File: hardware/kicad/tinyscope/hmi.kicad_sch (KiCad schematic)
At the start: 1 part, among them U10 CR2013-MI2120

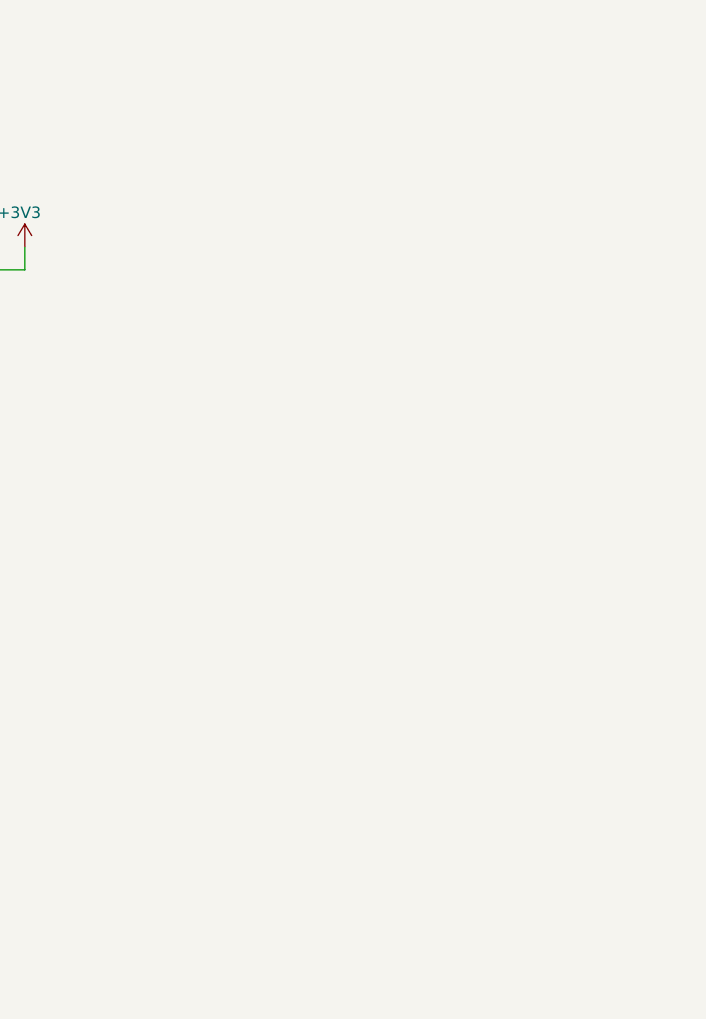
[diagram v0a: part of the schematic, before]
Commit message: feat: hardware: Adds five encoders in HMI schematic #1
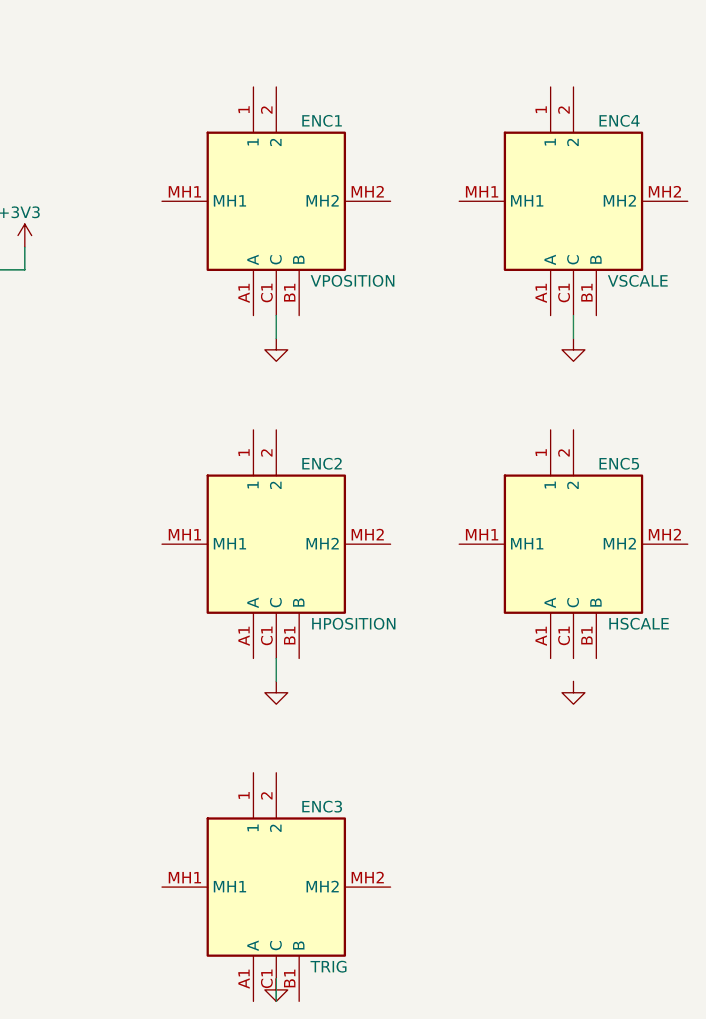
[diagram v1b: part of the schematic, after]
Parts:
- added ENC1: VPOSITION, PEC11R4220FS0024, symbol PEC11R-4220F-S0024:PEC11R-4220F-S0024
- added ENC2: HPOSITION, PEC11R4220FS0024, symbol PEC11R-4220F-S0024:PEC11R-4220F-S0024
- added ENC3: TRIG, PEC11R4220FS0024, symbol PEC11R-4220F-S0024:PEC11R-4220F-S0024
- added ENC4: VSCALE, PEC11R4220FS0024, symbol PEC11R-4220F-S0024:PEC11R-4220F-S0024
- added ENC5: HSCALE, PEC11R4220FS0024, symbol PEC11R-4220F-S0024:PEC11R-4220F-S0024
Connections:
- net GND: now also ENC1.C1 (C), ENC2.C1 (C), ENC3.C1 (C), ENC4.C1 (C)

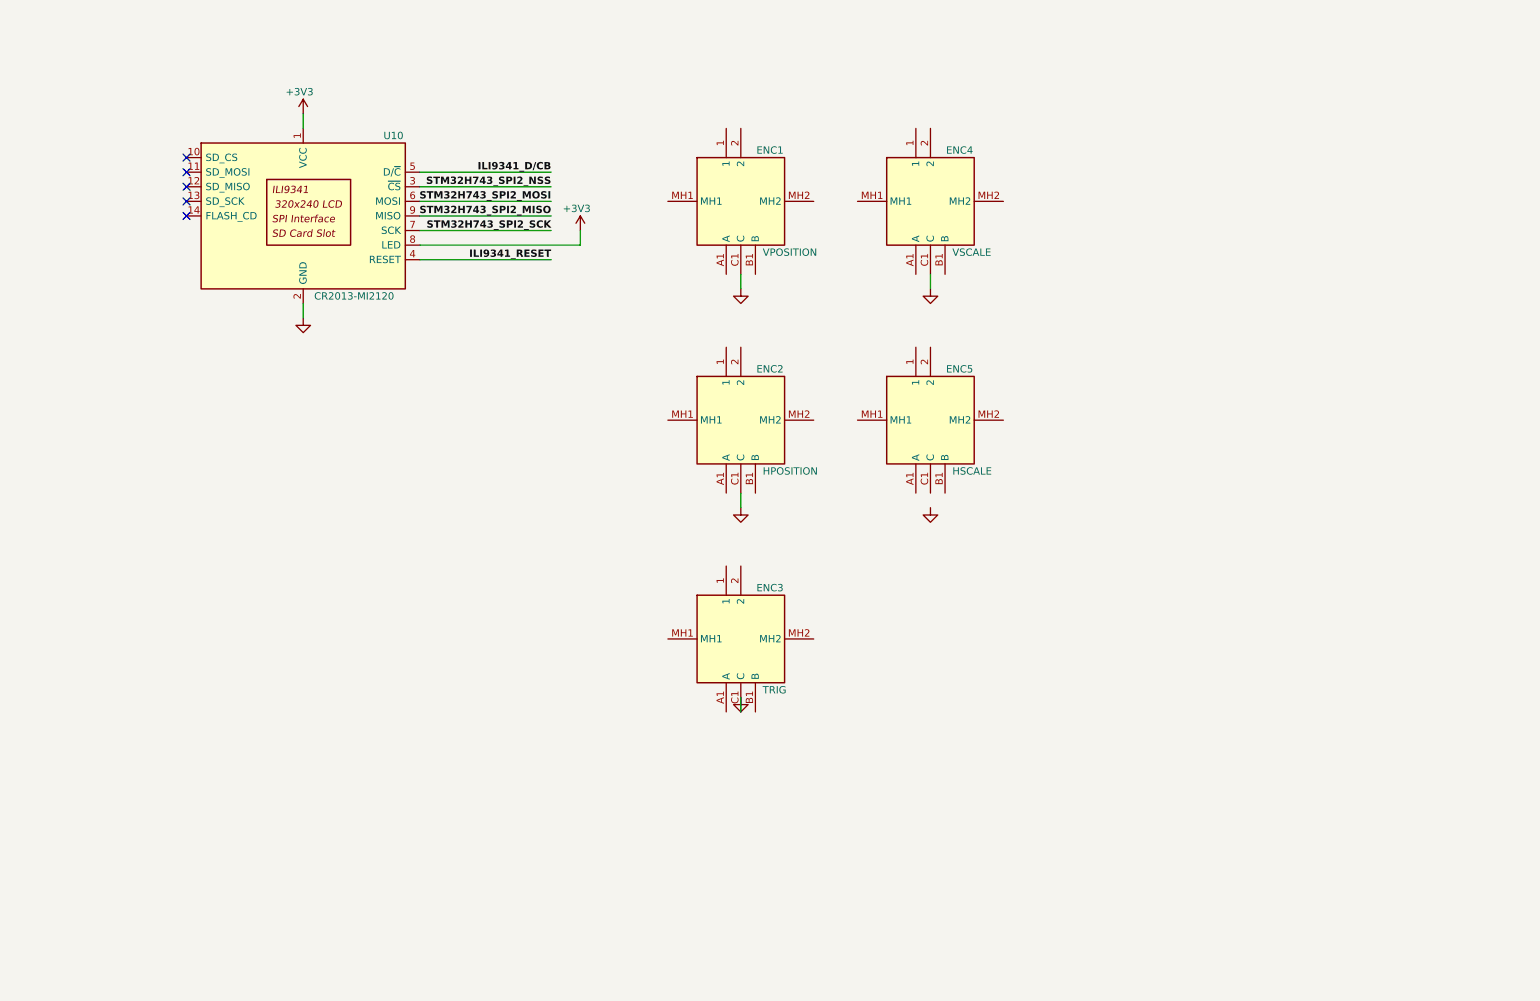
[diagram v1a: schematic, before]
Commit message: feat: hardware: Connects all five encoders to STM32H743
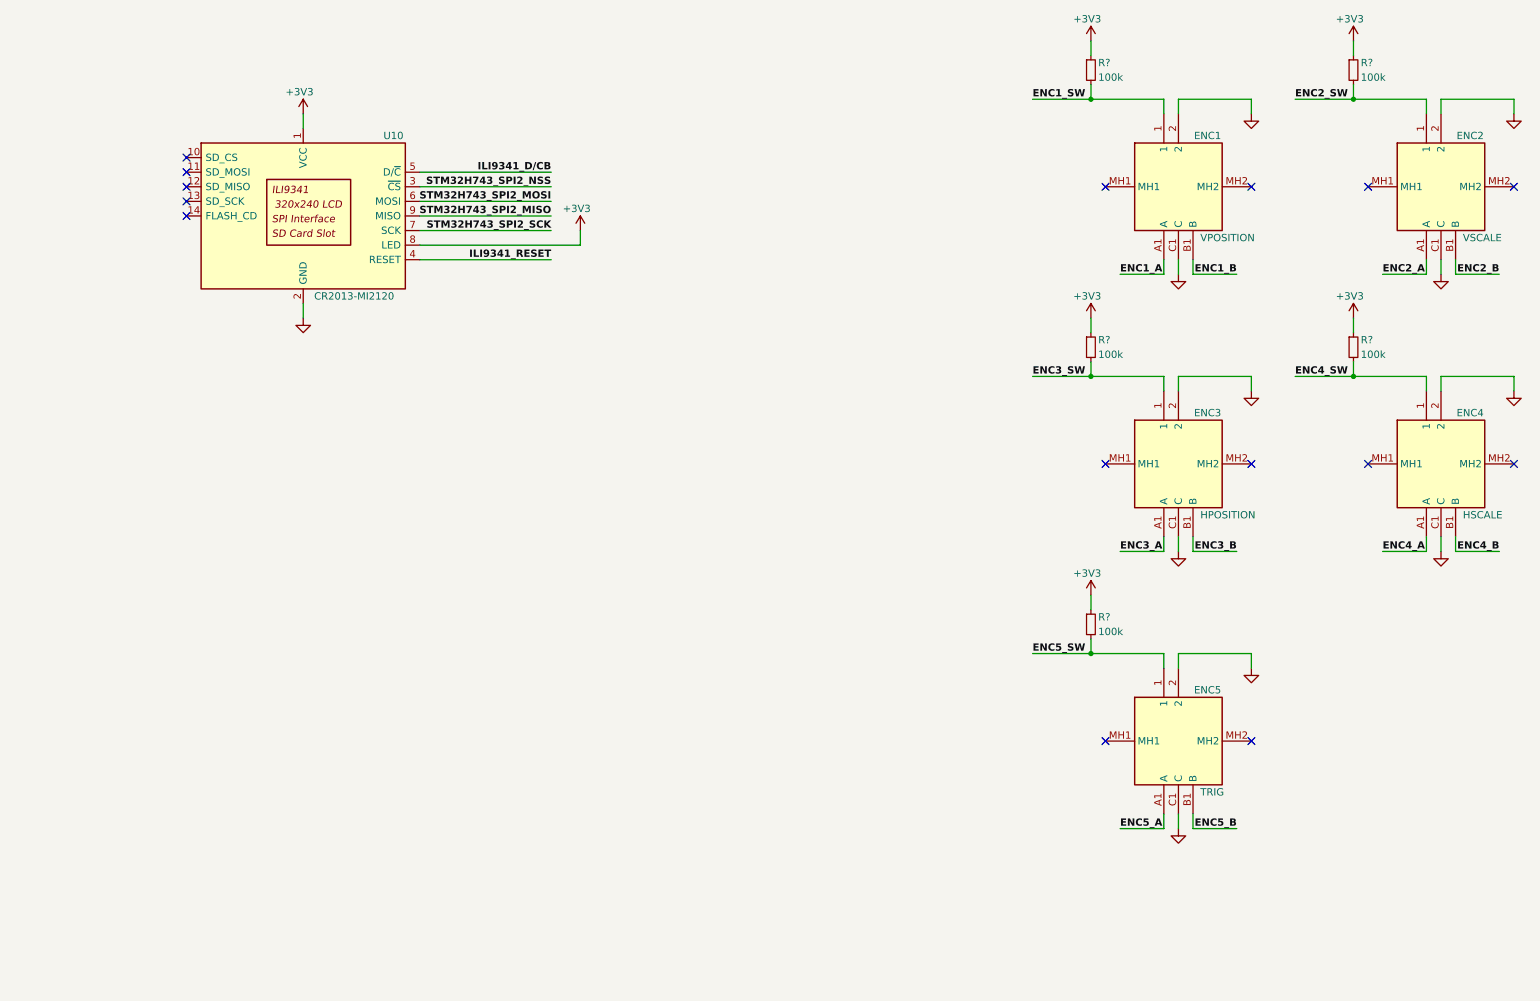
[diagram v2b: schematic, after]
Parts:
- added R? (x5): 100k, symbol Device:R_Small
- renumbered ENC4 to ENC2, ENC2 to ENC3, ENC5 to ENC4, ENC3 to ENC5
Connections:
- net +3V3: now also R?.1, R?.1, R?.1, R?.1, R?.1
- net GND: now also ENC1.2, ENC2.2, ENC3.2, ENC4.2, ENC4.C1 (C), ENC5.2
- net ENC3_SW: now reaches ENC3.1
- net ENC3_SW: now also R?.2
- net ENC3_A: now reaches ENC3.A1 (A)
- net ENC3_B: now reaches ENC3.B1 (B)
- net ENC1_SW: now reaches ENC1.1
- net ENC1_SW: now also R?.2
- net ENC1_A: now reaches ENC1.A1 (A)
- net ENC1_B: now reaches ENC1.B1 (B)
- net ENC5_SW: now reaches ENC5.1
- net ENC5_SW: now also R?.2
- net ENC5_A: now reaches ENC5.A1 (A)
- net ENC5_B: now reaches ENC5.B1 (B)
- net ENC2_SW: now reaches ENC2.1
- net ENC2_SW: now also R?.2
- net ENC2_A: now reaches ENC2.A1 (A)
- net ENC2_B: now reaches ENC2.B1 (B)
- net ENC4_SW: now reaches ENC4.1
- net ENC4_SW: now also R?.2
- net ENC4_A: now reaches ENC4.A1 (A)
- net ENC4_B: now reaches ENC4.B1 (B)
- no-connect marks 5 -> 15
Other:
- title: (none) -> HMI
- moved on the sheet: ENC1, ENC2, ENC3, ENC4, ENC5

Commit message: feat: hardware: Adds RC filters for each A/B channels for all encoders
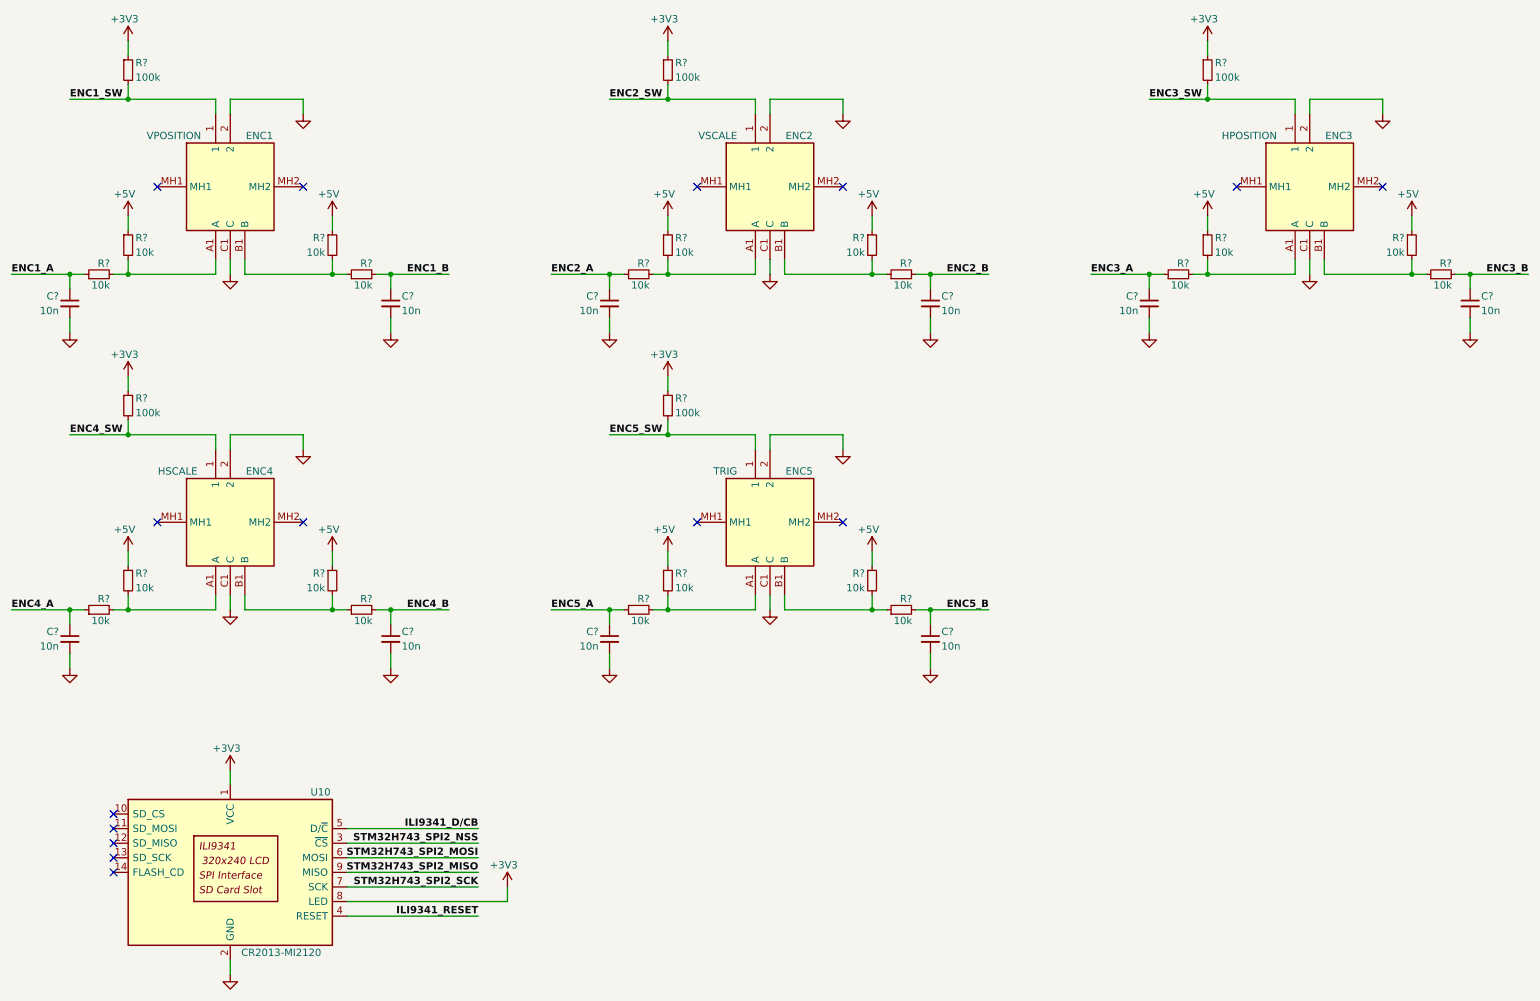
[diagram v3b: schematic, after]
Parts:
- removed R? (x4): 100k, symbol Device:R_Small
- added C? (x10): 10n, symbol Device:C_Small
- added R? (x20): 10k, symbol Device:R_Small
- added R? (x4): 100k, symbol Device:R_Small
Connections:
- net +3V3: now also R?.1, R?.1, R?.1, R?.1
- net ENC1_A: now also C?.1, R?.1; no longer ENC1.A1 (A)
- net ENC1_B: now also C?.1, R?.2; no longer ENC1.B1 (B)
- net ENC2_A: now also C?.1, R?.1; no longer ENC2.A1 (A)
- net ENC2_B: now also C?.1, R?.2; no longer ENC2.B1 (B)
- net ENC2_SW: now also R?.2
- net ENC3_A: now also C?.1, R?.1; no longer ENC3.A1 (A)
- net ENC3_B: now also C?.1, R?.2; no longer ENC3.B1 (B)
- net ENC3_SW: now also R?.2
- net ENC4_A: now also C?.1, R?.1; no longer ENC4.A1 (A)
- net ENC4_B: now also C?.1, R?.2; no longer ENC4.B1 (B)
- net ENC4_SW: now also R?.2
- net ENC5_A: now also C?.1, R?.1; no longer ENC5.A1 (A)
- net ENC5_B: now also C?.1, R?.2; no longer ENC5.B1 (B)
- net ENC5_SW: now also R?.2
- net GND: now also C?.2, C?.2, C?.2, C?.2, C?.2, C?.2, C?.2, C?.2, C?.2, C?.2
- new net: ENC2.A1 (A), R?.2, R?.2
- new net: ENC1.A1 (A), R?.2, R?.2
- new net: ENC2.B1 (B), R?.1, R?.2
- new net: ENC1.B1 (B), R?.1, R?.2
- new net: ENC3.B1 (B), R?.1, R?.2
- new net: ENC5.A1 (A), R?.2, R?.2
- new net: ENC4.B1 (B), R?.1, R?.2
- new net: ENC3.A1 (A), R?.2, R?.2
- new net: ENC5.B1 (B), R?.1, R?.2
- new net: ENC4.A1 (A), R?.2, R?.2
- new net +5V: R?.1, R?.1, R?.1, R?.1, R?.1, R?.1, R?.1, R?.1, R?.1, R?.1
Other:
- moved on the sheet: ENC1, R?, U10

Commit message: feat: hardware: Adds RC filters for each switches for all encoders
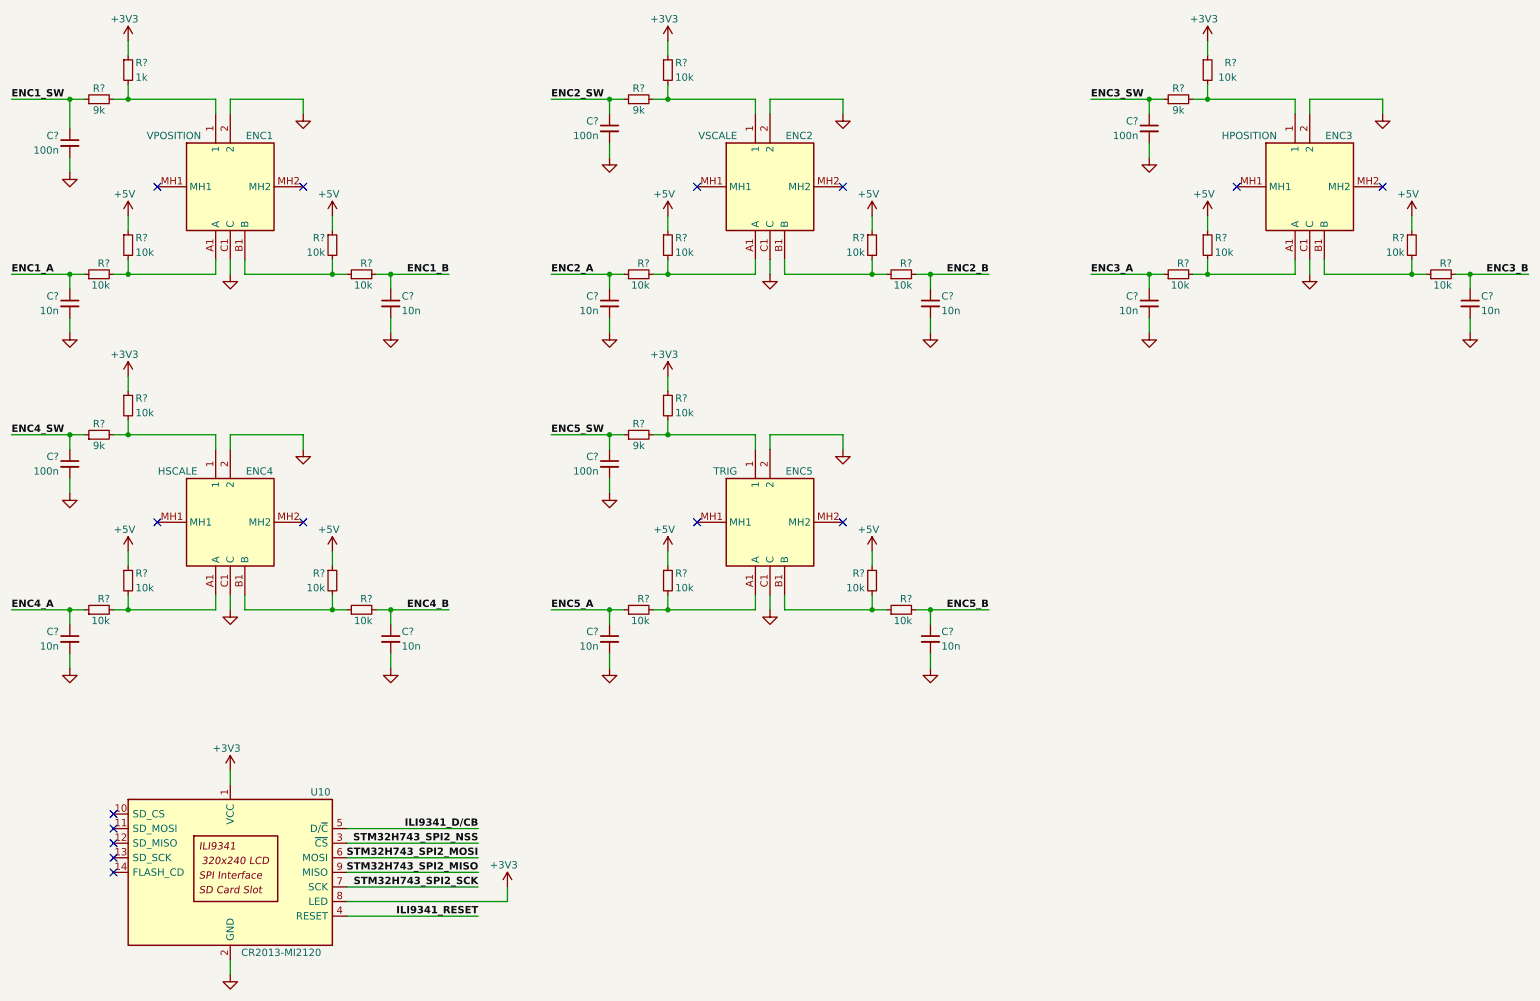
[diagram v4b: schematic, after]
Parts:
- added C? (x5): 100n, symbol Device:C_Small
- added R? (x5): 9k, symbol Device:R_Small
- R? (x4): value 100k -> 10k
- R?: value 100k -> 1k
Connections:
- net ENC1_SW: now also C?.1, R?.1; no longer ENC1.1, R?.2
- net ENC2_SW: now also C?.1, R?.1; no longer ENC2.1, R?.2
- net ENC3_SW: now also C?.1, R?.1; no longer ENC3.1, R?.2
- net ENC4_SW: now also C?.1, R?.1; no longer ENC4.1, R?.2
- net ENC5_SW: now also C?.1, R?.1; no longer ENC5.1, R?.2
- net GND: now also C?.2, C?.2, C?.2, C?.2, C?.2
- new net: ENC3.1, R?.2, R?.2
- new net: ENC1.1, R?.2, R?.2
- new net: ENC4.1, R?.2, R?.2
- new net: ENC5.1, R?.2, R?.2
- new net: ENC2.1, R?.2, R?.2
